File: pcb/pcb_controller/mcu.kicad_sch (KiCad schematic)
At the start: 32 parts, among them IC401 OPA277, J401 JST_XH_B2B-XH, J402 JST_XH_B4B-XH, J403 JST_XH_B4B-XH, J404 Goldpin_2x3, Q401 2N7002, Q402 2N7002, U401 REF3240, U402 MCP4725, U403 ATmega328P-A, U404 ADS1115IDGS, U405 MCP4725, Y401 16MHz

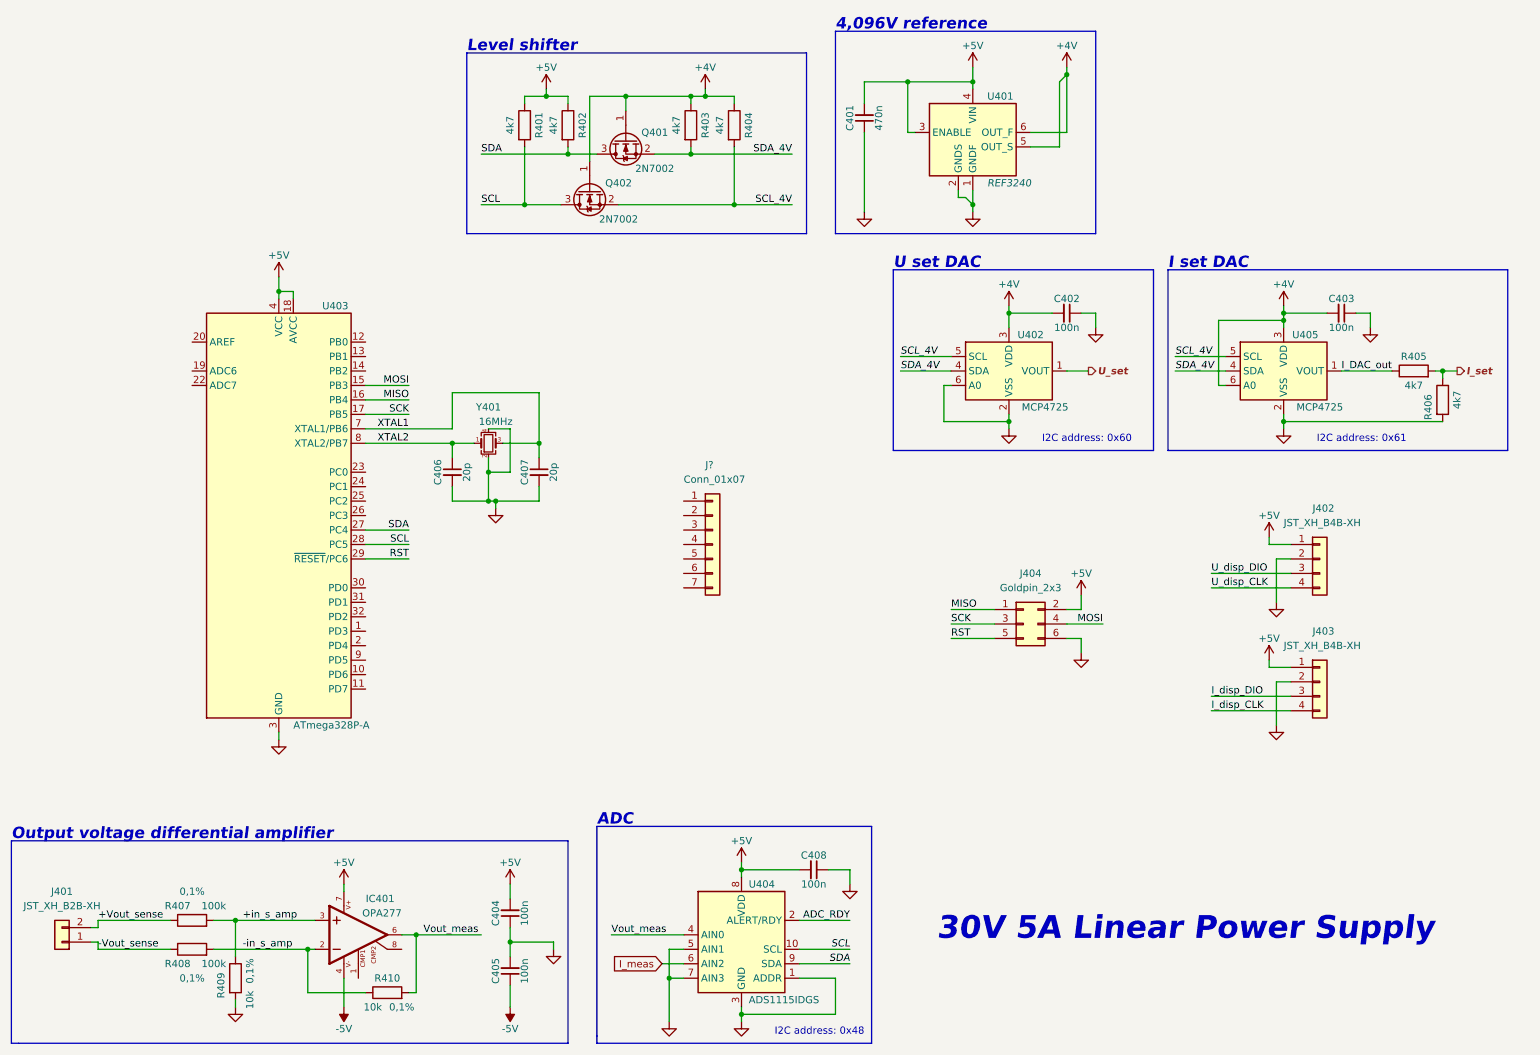
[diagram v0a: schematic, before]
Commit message: kicad 7.0, new design
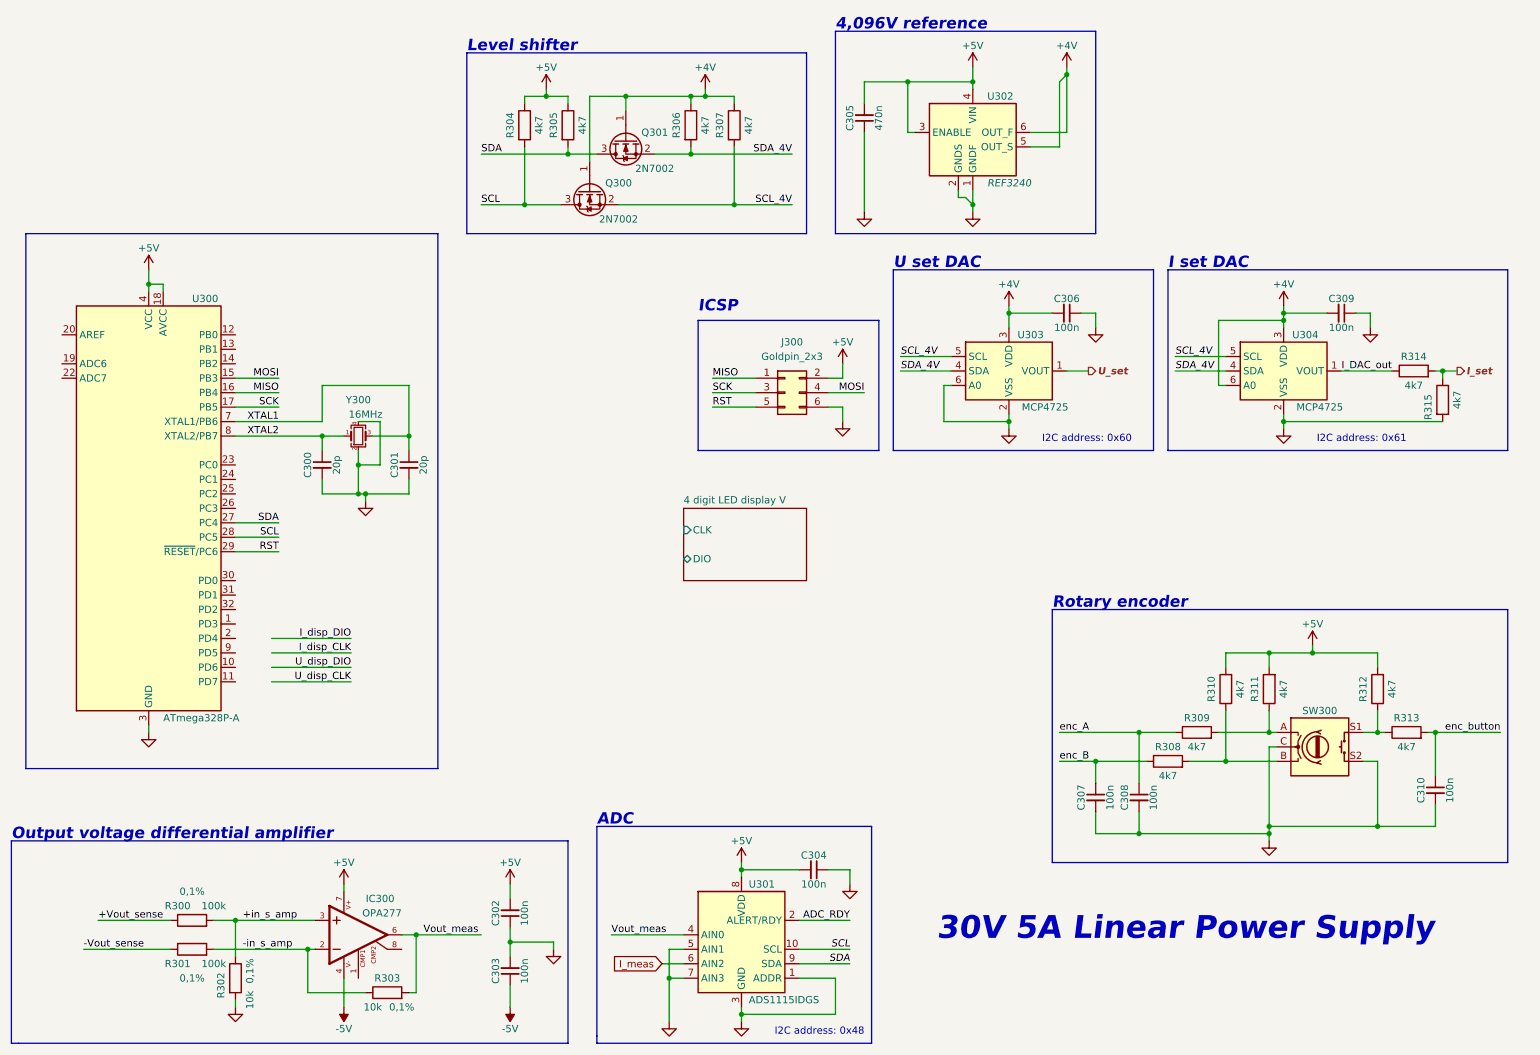
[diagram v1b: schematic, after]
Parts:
- removed C401: 470n, Capacitor_SMD:C_0603_1608Metric, symbol Device:C_Small
- removed C402, C403, C404, C405, C408: 100n, Capacitor_SMD:C_0603_1608Metric, symbol Device:C_Small
- removed C406, C407: 20p, Capacitor_SMD:C_0603_1608Metric, symbol Device:C_Small
- removed IC401: OPA277, OPA277:SO08, symbol OPA277:OPA277
- removed J401: JST_XH_B2B-XH, Connector_JST:JST_XH_B2B-XH-A_1x02_P2.50mm_Vertical, symbol Connector_Generic:Conn_01x02
- removed J402, J403: JST_XH_B4B-XH, Connector_JST:JST_XH_B4B-XH-A_1x04_P2.50mm_Vertical, symbol Connector_Generic:Conn_01x04
- removed J404: Goldpin_2x3, Connector_PinHeader_2.54mm:PinHeader_2x03_P2.54mm_Vertical, symbol Connector_Generic:Conn_02x03_Odd_Even
- removed J?: Conn_01x07, Connector_JST:JST_XH_B7B-XH-A_1x07_P2.50mm_Vertical, symbol Connector_Generic:Conn_01x07
- removed Q401, Q402: 2N7002, Package_TO_SOT_SMD:SOT-23, symbol Transistor_FET:2N7002
- removed R401, R402, R403, R404, R405, R406: 4k7, Resistor_SMD:R_0603_1608Metric, symbol Device:R
- removed R407, R408: 100k, Resistor_SMD:R_0603_1608Metric, symbol Device:R
- removed R409, R410: 10k, Resistor_SMD:R_0603_1608Metric, symbol Device:R
- removed U401: REF3240, Package_TO_SOT_SMD:SOT-23-6, symbol Reference_Voltage:REF3240AMDBVREP
- removed U402, U405: MCP4725, Package_TO_SOT_SMD:SOT-23-6, symbol Analog_DAC:MCP4725xxx-xCH
- removed U403: ATmega328P-A, Package_QFP:TQFP-32_7x7mm_P0.8mm, symbol MCU_Microchip_ATmega:ATmega328P-A
- removed U404: ADS1115IDGS, Package_SO:TSSOP-10_3x3mm_P0.5mm, symbol Analog_ADC:ADS1115IDGS
- removed Y401: 16MHz, Crystal:Crystal_SMD_SeikoEpson_TSX3225-4Pin_3.2x2.5mm, symbol Device:Crystal_GND24_Small
- added C300, C301: 20p, Capacitor_SMD:C_0603_1608Metric, symbol Device:C_Small
- added C302, C303, C304, C306, C307, C308, C309, C310: 100n, Capacitor_SMD:C_0603_1608Metric, symbol Device:C_Small
- added C305: 470n, Capacitor_SMD:C_0603_1608Metric, symbol Device:C_Small
- added IC300: OPA277, OPA277:SO08, symbol OPA277:OPA277
- added J300: Goldpin_2x3, Connector_PinHeader_2.54mm:PinHeader_2x03_P2.54mm_Vertical, symbol Connector_Generic:Conn_02x03_Odd_Even
- added Q300, Q301: 2N7002, Package_TO_SOT_SMD:SOT-23, symbol Transistor_FET:2N7002
- added R300, R301: 100k, Resistor_SMD:R_0603_1608Metric, symbol Device:R
- added R302, R303: 10k, Resistor_SMD:R_0603_1608Metric, symbol Device:R
- added R304, R305, R306, R307, R308, R309, R310, R311, R312, R313, R314, R315: 4k7, Resistor_SMD:R_0603_1608Metric, symbol Device:R
- added SW300: RotaryEncoder_Switch, Rotary_Encoder:RotaryEncoder_Alps_EC11E-Switch_Vertical_H20mm, symbol Device:RotaryEncoder_Switch
- added U300: ATmega328P-A, Package_QFP:TQFP-32_7x7mm_P0.8mm, symbol MCU_Microchip_ATmega:ATmega328P-A
- added U301: ADS1115IDGS, Package_SO:TSSOP-10_3x3mm_P0.5mm, symbol Analog_ADC:ADS1115IDGS
- added U302: REF3240, Package_TO_SOT_SMD:SOT-23-6, symbol Reference_Voltage:REF3240AMDBVREP
- added U303, U304: MCP4725, Package_TO_SOT_SMD:SOT-23-6, symbol Analog_DAC:MCP4725xxx-xCH
- added Y300: 16MHz, Crystal:Crystal_SMD_SeikoEpson_TSX3225-4Pin_3.2x2.5mm, symbol Device:Crystal_GND24_Small
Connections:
- net +4V: now also C306.2, C309.2, Q300.1 (G), Q301.1 (G), R306.1, R307.1, U302.5 (OUT_S), U302.6 (OUT_F), U303.3 (VDD), U304.3 (VDD), U304.6 (A0)
- net +5V: now also C302.2, C304.2, C305.2, IC300.7, J300.2 (Pin_2), R304.1, R305.1, R310.2, R311.2, R312.2, U300.18 (AVCC), U300.4 (VCC), U300.6 (VCC), U301.8 (VDD), U302.3 (ENABLE), U302.4 (VIN)
- net +Vout_sense: now also R300.1
- net +in_s_amp: now also IC300.3, R300.2, R302.1
- net -5V: now also C303.1, IC300.4
- net -Vout_sense: now also R301.1
- net -in_s_amp: now also IC300.2, R301.2, R303.1
- net ADC_RDY: now also U301.2 (ALERT/RDY)
- net GND: now also C300.2, C301.2, C302.1, C303.2, C304.1, C305.1, C306.1, C307.2, C308.2, C309.1, C310.2, J300.6 (Pin_6), R302.2, R315.2, SW300.C, SW300.S2, U300.21 (GND), U300.3 (GND), U300.5 (GND), U301.1 (ADDR), U301.3 (GND), U301.5 (AIN1), U301.7 (AIN3), U302.1 (GNDF), U302.2 (GNDS), U303.2 (VSS), U303.6 (A0), U304.2 (VSS), Y300.2, Y300.4
- net I_DAC_out: now also R314.1, U304.1 (VOUT)
- net I_meas: now also U301.6 (AIN2)
- net I_set: now also R314.2, R315.1
- net MISO: now also J300.1 (Pin_1), U300.16 (PB4)
- net MOSI: now also J300.4 (Pin_4), U300.15 (PB3)
- net RST: now also J300.5 (Pin_5), U300.29 (~{RESET}/PC6)
- net SCK: now also J300.3 (Pin_3), U300.17 (PB5)
- net SCL: now also Q300.3 (D), R304.2, U300.28 (PC5), U301.10 (SCL)
- net SCL_4V: now also Q300.2 (S), R307.2, U303.5 (SCL), U304.5 (SCL)
- net SDA: now also Q301.3 (D), R305.2, U300.27 (PC4), U301.9 (SDA)
- net SDA_4V: now also Q301.2 (S), R306.2, U303.4 (SDA), U304.4 (SDA)
- net U_set: now also U303.1 (VOUT)
- net Vout_meas: now also IC300.6, R303.2, U301.4 (AIN0)
- net XTAL1: now also C301.1, U300.7 (XTAL1/PB6), Y300.3
- net XTAL2: now also C300.1, U300.8 (XTAL2/PB7), Y300.1
- new net: R312.1, R313.1, SW300.S1
- new net: R308.2, R310.1, SW300.B
- new net: R309.2, R311.1, SW300.A
- new net enc_A: C308.1, R309.1
- new net enc_B: C307.1, R308.1
- new net enc_button: C310.1, R313.2
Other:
- added sheet 4 digit LED display V (led_display_V.kicad_sch)
- note added: "ICSP"
- note added: "Rotary encoder"
- company: Dominik Workshop -> (none)
- title: MCU + DAC + ADC -> (none)

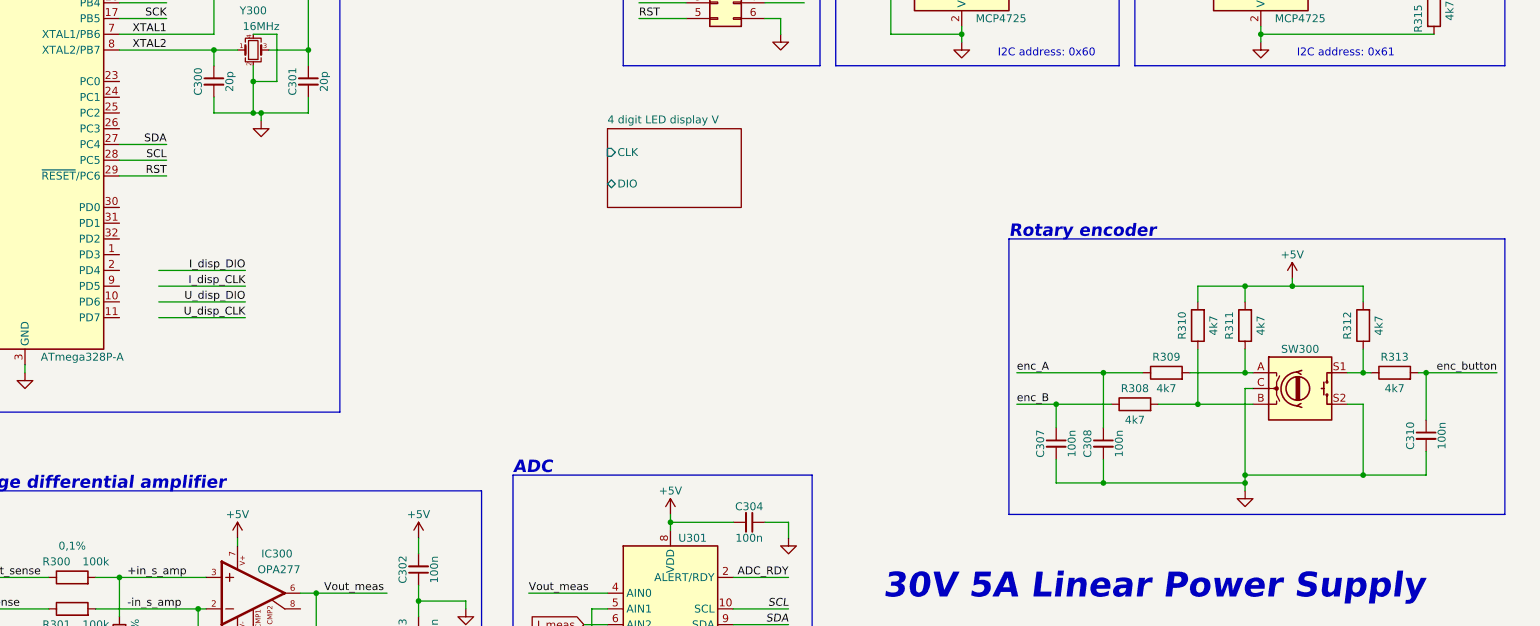
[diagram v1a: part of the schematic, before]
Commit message: kicad 8.0
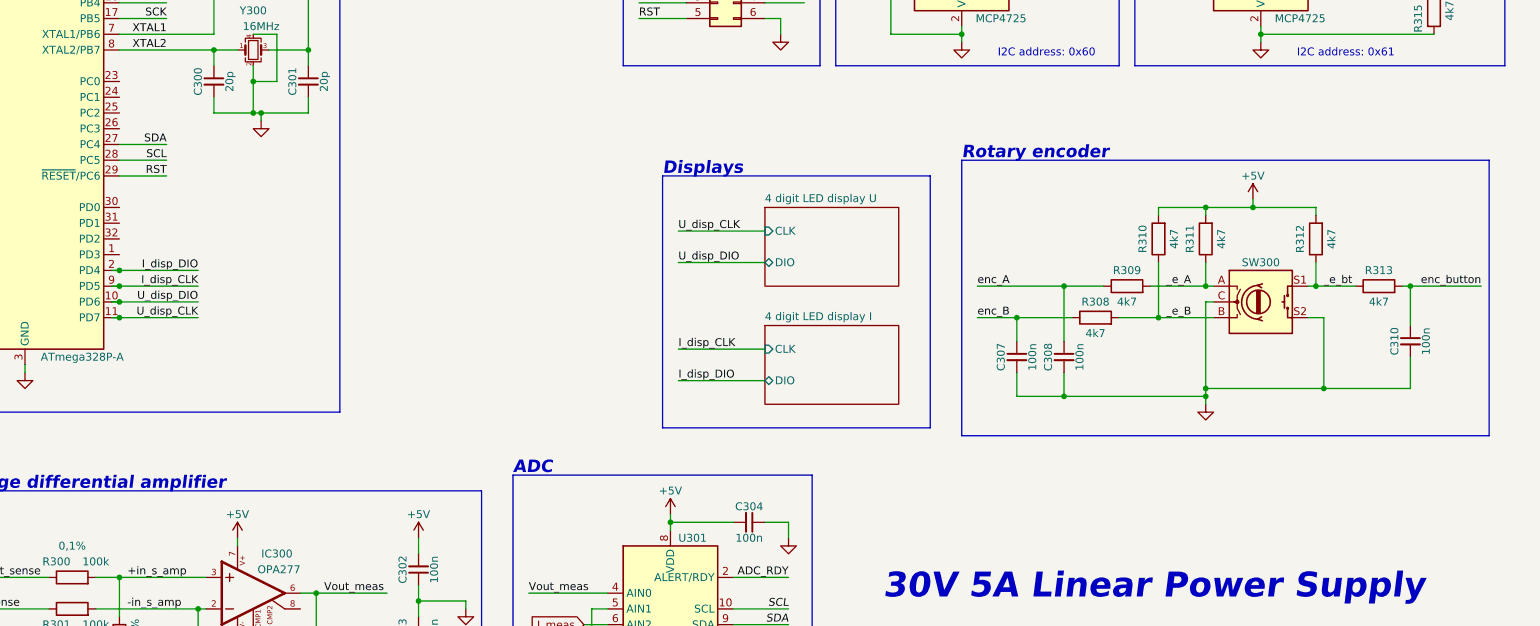
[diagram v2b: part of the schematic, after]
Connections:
- net I_disp_CLK: now also U300.9 (PD5)
- net I_disp_DIO: now also U300.2 (PD4)
- net U_disp_CLK: now also U300.11 (PD7)
- net U_disp_DIO: now also U300.10 (PD6)
- net _e_bt: now reaches R312.1, R313.1, SW300.S1
- net _e_B: now reaches R308.2, R310.1, SW300.B
- net _e_A: now reaches R309.2, R311.1, SW300.A
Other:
- sheet 4 digit LED display V renamed 4 digit LED display U
- added sheet 4 digit LED display I (led_display_I.kicad_sch)
- sheet 4 digit LED display U: file led_display_V.kicad_sch -> led_display_U.kicad_sch
- note added: "Displays"
- company: (none) -> Dominik Workshop
- title: (none) -> MCU, DAC, ADC, display, encoder
- moved on the sheet: C307, C308, C310, R308, R309, R310, R311, R312, R313, SW300

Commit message: most analog layout
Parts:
- added J301: JST_XH_B3B-XH, Connector_JST:JST_XH_B3B-XH-A_1x03_P2.50mm_Vertical, symbol Connector_Generic:Conn_01x03
- added Q302, Q305: CJ2306, Package_TO_SOT_SMD:SOT-23, symbol Transistor_FET:2N7002
- added Q303: 2N7002, Package_TO_SOT_SMD:SOT-23, symbol Transistor_FET:2N7002
- added Q304: BSS83P, Package_TO_SOT_SMD:SOT-23, symbol Transistor_FET:BSS83P
- added R314, R315, R319: 220R, Resistor_SMD:R_0603_1608Metric, symbol Device:R
- added R316, R317, R318, R320, R321: 10k, Resistor_SMD:R_0603_1608Metric, symbol Device:R
- renumbered C307 to C300, C308 to C301, C300 to C302, C301 to C303, C310 to C304, C302 to C307, C303 to C308, C304 to C310, R308 to R300, R309 to R301, R310 to R302, R311 to R303, R312 to R304, R313 to R305, R304 to R306, R305 to R307, R306 to R308, R307 to R309, R300 to R310, R301 to R311, R302 to R312, R303 to R313, R314 to R322, R315 to R323, U302 to U301, U303 to U302, U304 to U303, U301 to U304
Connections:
- net GND: now also J301.1 (Pin_1), Q302.2 (S), Q303.2 (S), Q305.2 (S), R316.2, R317.2, R321.2
- new net +12V: Q304.2 (S), R318.1, R320.1
- new net fan_pwm: R315.2
- new net fan_tacho: J301.3 (Pin_3), R320.2
- new net fan_v+: J301.2 (Pin_2), Q304.3 (D)
- new net fpwm_g: Q303.3 (D), Q304.1 (G), R318.2
- new net fpwm_r: Q303.1 (G), R315.1, R317.1
- new net r1g_r: Q302.1 (G), R314.1, R316.1
- new net r2g_r: Q305.1 (G), R319.1, R321.1
- new net relay1: Q302.3 (D)
- new net relay2: Q305.3 (D)
- new net relay_1_g: R314.2
- new net relay_2_g: R319.2
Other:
- note added: "Output voltage differential amplifier k=1/10"
- note removed: "Output voltage differential amplifier"
- moved on the sheet: C300, C301, C302, C303, C304, C305, C306, C307, C308, C309, C310, IC300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

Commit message: minor changes
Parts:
- added C311, C312, C313: 100n, Capacitor_SMD:C_0603_1608Metric, symbol Device:C_Small
- added J302: JST_XH_B3B-XH, Connector_JST:JST_XH_B3B-XH-A_1x03_P2.50mm_Vertical, symbol Connector_Generic:Conn_01x03
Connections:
- net +12V: no longer R320.1
- net +5V: now also R320.1, C311.1, C312.1
- net GND: now also C311.2, C312.2, C313.2, J302.1 (Pin_1)
- net at U300.20 (AREF): now also C313.1
- net RX: now reaches U300.30 (PD0)
- net RX: now also J302.3 (Pin_3)
- net TX: now reaches U300.31 (PD1)
- net TX: now also J302.2 (Pin_2)
- net Out_on: now reaches U300.32 (PD2)
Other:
- note added: "Cooling fan with tachometer"
- note added: "MCU"
- note added: "Tab switching relays driver"
- note added: "UART"
- moved on the sheet: C300, C301, C302, C303, C304, C305, C306, C307, C308, C309, C310, IC300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
